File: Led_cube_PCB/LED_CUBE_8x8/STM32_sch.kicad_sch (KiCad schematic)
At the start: 23 parts, among them IC29 STM32C071C8T6, IC30 TPS562202DRLR, J2 20021121-00014T4LF, Y1 ABM11-48.000MHz-D7X-T

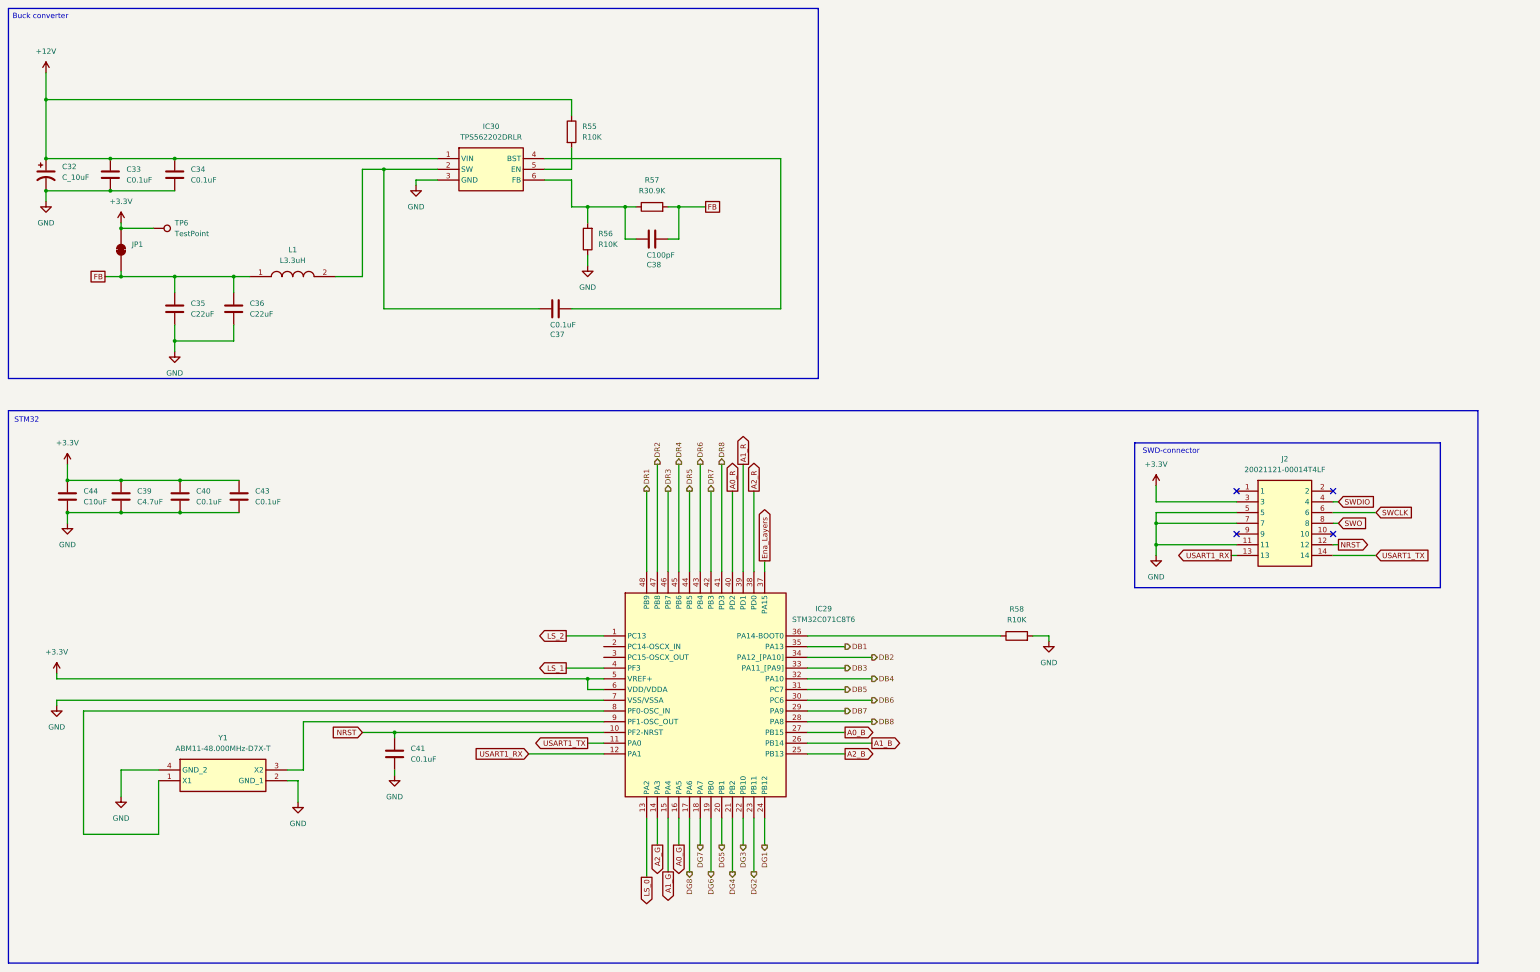
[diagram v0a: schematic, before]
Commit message: Finalized schematic changed power source and buck converter due to unavailability stock mouser. Also assigned all the footprints to all components and ran ERC.
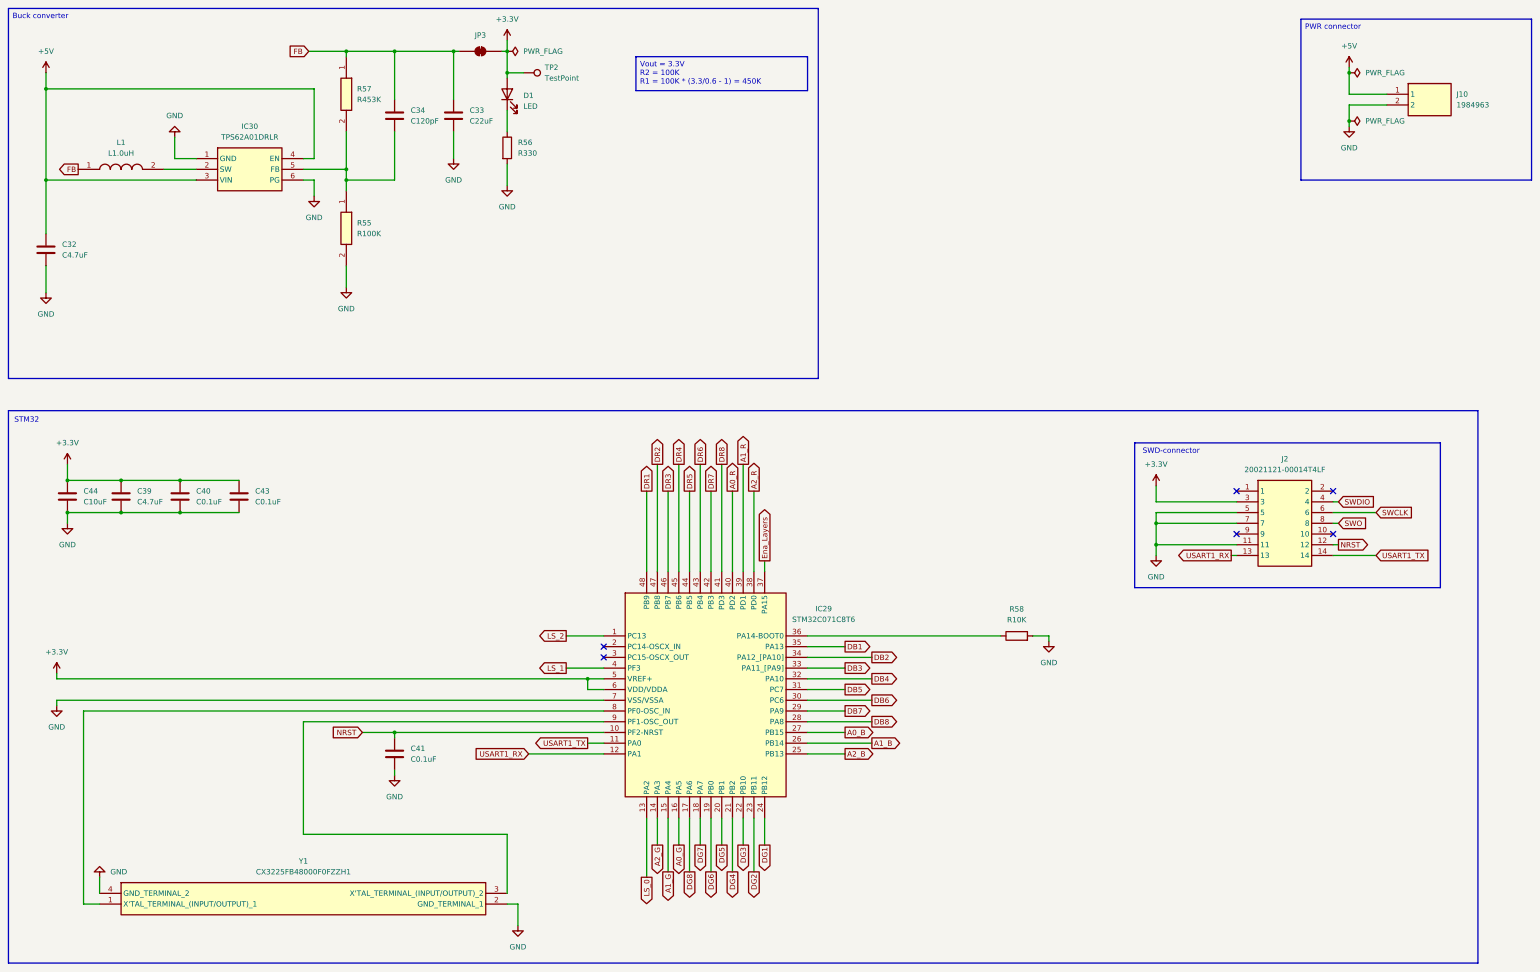
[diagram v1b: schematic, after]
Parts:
- removed C32: C_10uF, symbol Device:C_Polarized_US
- removed C35, C36: C22uF, symbol Device:C
- removed C37: C0.1uF, symbol Device:C
- removed C38: C100pF, symbol Device:C
- removed IC30: TPS562202DRLR, SOTFL50P160X60-6N, symbol SamacSys_Parts:TPS562202DRLR
- removed JP1: SolderJumper_2_Bridged, Jumper:SolderJumper-2_P1.3mm_Open_RoundedPad1.0x1.5mm, symbol Jumper:SolderJumper_2_Bridged
- removed L1: L3.3uH, BMRA000606303R3MA1, symbol SamacSys_Parts:BMRA000606303R3MA1
- removed R55: R10K, symbol Device:R
- removed R57: R30.9K, symbol Device:R
- removed TP6: TestPoint, TestPoint:TestPoint_Pad_D2.0mm, symbol Connector:TestPoint
- removed Y1: ABM11-48.000MHz-D7X-T, ABM11, symbol SamacSys_Parts:ABM11-48.000MHz-D7X-T
- added C32: C4.7uF, Capacitor_SMD:C_0805_2012Metric_Pad1.18x1.45mm_HandSolder, symbol Device:C
- added D1: LED, LED_SMD:LED_0805_2012Metric_Pad1.15x1.40mm_HandSolder, symbol Device:LED
- added IC30: TPS62A01DRLR, SamacSys_Parts:SOTFL50P160X60-6N, symbol SamacSys_Parts:TPS62A01DRLR
- added J10: 1984963, SamacSys_Parts:1984963, symbol SamacSys_Parts:1984963
- added JP3: SolderJumper_2_Bridged, Jumper:SolderJumper-2_P1.3mm_Open_RoundedPad1.0x1.5mm, symbol Jumper:SolderJumper_2_Bridged
- added L1: L1.0uH, SamacSys_Parts:DFE2HCAH1R0MJ0L, symbol SamacSys_Parts:DFE252012F-1R0M=P2
- added R55: R100K, Resistor_SMD:R_0805_2012Metric_Pad1.20x1.40mm_HandSolder, symbol SamacSys_Parts:RC0201FR-7D100KL
- added R57: R453K, Resistor_SMD:R_0805_2012Metric_Pad1.20x1.40mm_HandSolder, symbol SamacSys_Parts:RC0201FR-07453KL
- added TP2: TestPoint, TestPoint:TestPoint_Pad_D2.0mm, symbol Connector:TestPoint
- added Y1: CX3225FB48000F0FZZH1, SamacSys_Parts:CX3225FB48000F0FZZH1, symbol SamacSys_Parts:CX3225FB48000F0FZZH1
- C33: value C0.1uF -> C22uF; footprint (none) -> Capacitor_SMD:C_0805_2012Metric_Pad1.18x1.45mm_HandSolder
- C34: value C0.1uF -> C120pF; footprint (none) -> Capacitor_SMD:C_0805_2012Metric_Pad1.18x1.45mm_HandSolder
- C39, C40, C41, C43, C44: footprint (none) -> Capacitor_SMD:C_0805_2012Metric_Pad1.18x1.45mm_HandSolder
- IC29: footprint QFP50P900X900X160-48N -> SamacSys_Parts:QFP50P900X900X160-48N
- J2: footprint 2002112100014T4LF -> SamacSys_Parts:2002112100014T4LF
- R56: value R10K -> R330; footprint (none) -> Resistor_SMD:R_0805_2012Metric_Pad1.20x1.40mm_HandSolder
- R58: footprint (none) -> Resistor_SMD:R_0805_2012Metric_Pad1.20x1.40mm_HandSolder
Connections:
- net +12V is gone; now on net FB: C33.1, C34.1
- net +3.3V: now also D1.2 (A), JP3.1 (A), TP2.1
- net FB: now also JP3.2 (B), L1.1, R57.1
- net GND: now also R56.2, C32.2, IC30.1 (GND), IC30.6 (PG), J10.2, R55.2, Y1.2 (GND_TERMINAL_1), Y1.4 (GND_TERMINAL_2); no longer C34.2, R56.1
- net at IC29.8 (PF0-OSC_IN): now also Y1.1 (X'TAL_TERMINAL_(INPUT/OUTPUT)_1)
- net at IC29.9 (PF1-OSC_OUT): now also Y1.3 (X'TAL_TERMINAL_(INPUT/OUTPUT)_2)
- new net: C34.2, IC30.5 (FB), R55.1, R57.2
- new net: D1.1 (K), R56.1
- new net: IC30.2 (SW), L1.2
- new net +5V: C32.1, IC30.3 (VIN), IC30.4 (EN), J10.1
- no-connect marks 4 -> 6

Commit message: start of PCB layout
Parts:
- C32, C33, C34, C39, C40, C41, C43, C44: footprint Capacitor_SMD:C_0805_2012Metric_Pad1.18x1.45mm_HandSolder -> Capacitor_SMD:C_0603_1608Metric_Pad1.08x0.95mm_HandSolder
- R55: footprint Resistor_SMD:R_0805_2012Metric_Pad1.20x1.40mm_HandSolder -> Resistor_SMD:R_0603_1608Metric_Pad0.98x0.95mm_HandSolder; Manufacturer_Part_Number RC0201FR-7D100KL -> SR0603FR-07100KL; Mouser Part Number 603-RC0201FR-7D100KL -> 603-SR0603FR-07100KL; Mouser Price/Stock https://www.mouser.co.uk/ProductDetail/YAGEO/RC0201FR-7D100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 -> https://nl.mouser.com/en/ProductDetail/YAGEO/SR0603FR-07100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
- R56, R58: footprint Resistor_SMD:R_0805_2012Metric_Pad1.20x1.40mm_HandSolder -> Resistor_SMD:R_0603_1608Metric_Pad0.98x0.95mm_HandSolder
- R57: footprint Resistor_SMD:R_0805_2012Metric_Pad1.20x1.40mm_HandSolder -> Resistor_SMD:R_0603_1608Metric_Pad0.98x0.95mm_HandSolder; Manufacturer_Part_Number RC0201FR-07453KL -> AF0603FR-07453KL; Mouser Part Number 603-RC0201FR-07453KL -> 603-AF0603FR-07453KL; Mouser Price/Stock https://www.mouser.co.uk/ProductDetail/YAGEO/RC0201FR-07453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 -> https://nl.mouser.com/en/ProductDetail/YAGEO/AF0603FR-07453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
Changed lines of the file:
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@@
 			)
 		)
-		(property "Footprint" "Capacitor_SMD:C_0805_2012Metric_Pad1.18x1.45mm_HandSolder"
+		(property "Footprint" "Capacitor_SMD:C_0603_1608Metric_Pad1.08x0.95mm_HandSolder"
 			(at 56.8452 133.35 0)
 			(hide yes)
@@
 			)
 		)
-		(property "Footprint" "Resistor_SMD:R_0805_2012Metric_Pad1.20x1.40mm_HandSolder"
+		(property "Footprint" "Resistor_SMD:R_0603_1608Metric_Pad0.98x0.95mm_HandSolder"
 			(at -0.94 71.12 0)
 			(hide yes)
@@
 			)
 		)
-		(property "Datasheet" "http://www.yageo.com/documents/recent/PYu-RC0201_51_RoHS_L_8.pdf"
+		(property "Datasheet" ""
 			(at -100.94 71.12 0)
 			(hide yes)
@@
 			)
 		)
-		(property "Mouser Part Number" "603-RC0201FR-7D100KL"
+		(property "Mouser Part Number" "603-SR0603FR-07100KL"
 			(at -400.94 71.12 0)
 			(hide yes)
@@
 			)
 		)
-		(property "Mouser Price/Stock" "https://www.mouser.co.uk/ProductDetail/YAGEO/RC0201FR-7D100KL?qs=NgbZBzc1CyEJ6dcGr2%2F%252Bdg%3D%3D"
+		(property "Mouser Price/Stock" "https://nl.mouser.com/en/ProductDetail/YAGEO/SR0603FR-07100KL?qs=sGAEpiMZZMtG0KNrPCHnjRv1MJzRlXPZ3DN8ub9uSdtrODw9zR96PQ%3D%3D"
 			(at -500.94 71.12 0)
 			(hide yes)
@@
 			)
 		)
-		(property "Manufacturer_Part_Number" "RC0201FR-7D100KL"
+		(property "Manufacturer_Part_Number" "SR0603FR-07100KL"
 			(at -700.94 71.12 0)
 			(hide yes)
@@
 			)
 		)
-		(property "Footprint" "Capacitor_SMD:C_0805_2012Metric_Pad1.18x1.45mm_HandSolder"
+		(property "Footprint" "Capacitor_SMD:C_0603_1608Metric_Pad1.08x0.95mm_HandSolder"
 			(at 107.6452 194.31 0)
 			(hide yes)
@@
 			)
 		)
-		(property "Footprint" "Capacitor_SMD:C_0805_2012Metric_Pad1.18x1.45mm_HandSolder"
+		(property "Footprint" "Capacitor_SMD:C_0603_1608Metric_Pad1.08x0.95mm_HandSolder"
 			(at 42.8752 133.35 0)
 			(hide yes)
@@
 			)
 		)
-		(property "Footprint" "Resistor_SMD:R_0805_2012Metric_Pad1.20x1.40mm_HandSolder"
+		(property "Footprint" "Resistor_SMD:R_0603_1608Metric_Pad0.98x0.95mm_HandSolder"
 			(at 254 164.338 90)
 			(hide yes)
@@
 			)
 		)
-		(property "Footprint" "Capacitor_SMD:C_0805_2012Metric_Pad1.18x1.45mm_HandSolder"
+		(property "Footprint" "Capacitor_SMD:C_0603_1608Metric_Pad1.08x0.95mm_HandSolder"
 			(at 70.8152 133.35 0)
 			(hide yes)
@@
 			)
 		)
-		(property "Footprint" "Capacitor_SMD:C_0805_2012Metric_Pad1.18x1.45mm_HandSolder"
+		(property "Footprint" "Capacitor_SMD:C_0603_1608Metric_Pad1.08x0.95mm_HandSolder"
 			(at 25.0952 74.93 0)
 			(hide yes)
@@
 			)
 		)
-		(property "Footprint" "Capacitor_SMD:C_0805_2012Metric_Pad1.18x1.45mm_HandSolder"
+		(property "Footprint" "Capacitor_SMD:C_0603_1608Metric_Pad1.08x0.95mm_HandSolder"
 			(at 107.6452 43.18 0)
 			(hide yes)
@@
 			)
 		)
-		(property "Footprint" "Capacitor_SMD:C_0805_2012Metric_Pad1.18x1.45mm_HandSolder"
+		(property "Footprint" "Capacitor_SMD:C_0603_1608Metric_Pad1.08x0.95mm_HandSolder"
 			(at 121.6152 43.18 0)
 			(hide yes)
@@
 			)
 		)
-		(property "Footprint" "Capacitor_SMD:C_0805_2012Metric_Pad1.18x1.45mm_HandSolder"
+		(property "Footprint" "Capacitor_SMD:C_0603_1608Metric_Pad1.08x0.95mm_HandSolder"
 			(at 30.1752 133.35 0)
 			(hide yes)
@@
 			)
 		)
-		(property "Footprint" "Resistor_SMD:R_0805_2012Metric_Pad1.20x1.40mm_HandSolder"
+		(property "Footprint" "Resistor_SMD:R_0603_1608Metric_Pad0.98x0.95mm_HandSolder"
 			(at 131.572 46.99 90)
 			(hide yes)
@@
 			)
 		)
-		(property "Footprint" "Resistor_SMD:R_0805_2012Metric_Pad1.20x1.40mm_HandSolder"
+		(property "Footprint" "Resistor_SMD:R_0603_1608Metric_Pad0.98x0.95mm_HandSolder"
 			(at -0.94 39.37 0)
 			(hide yes)
@@
 			)
 		)
-		(property "Datasheet" "https://www.yageo.com/upload/media/product/products/datasheet/rchip/PYu-RC_Group_51_RoHS_L_12.pdf"
+		(property "Datasheet" "chrome-extension://efaidnbmnnnibpcajpcglclefindmkaj/https://nl.mouser.com/datasheet/3/508/1/PYu-AF_51_RoHS_L_9.pdf"
 			(at -100.94 39.37 0)
 			(hide yes)
@@
 			)
 		)
-		(property "Mouser Part Number" "603-RC0201FR-07453KL"
+		(property "Mouser Part Number" "603-AF0603FR-07453KL"
 			(at -400.94 39.37 0)
 			(hide yes)
@@
 			)
 		)
-		(property "Mouser Price/Stock" "https://www.mouser.co.uk/ProductDetail/YAGEO/RC0201FR-07453KL?qs=1s%252BlIcjv25sZ2i87AF%252BnmQ%3D%3D"
+		(property "Mouser Price/Stock" "https://nl.mouser.com/en/ProductDetail/YAGEO/AF0603FR-07453KL?qs=sGAEpiMZZMtlubZbdhIBIK%252BAKCop5cydMz3xptmMHDE%3D"
 			(at -500.94 39.37 0)
 			(hide yes)
@@
 			)
 		)
-		(property "Manufacturer_Part_Number" "RC0201FR-07453KL"
+		(property "Manufacturer_Part_Number" "AF0603FR-07453KL"
 			(at -700.94 39.37 0)
 			(hide yes)

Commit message: Top layer placement done revised the SWD connector and started routing.
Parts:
- removed C44: C10uF, Capacitor_SMD:C_0603_1608Metric_Pad1.08x0.95mm_HandSolder, symbol Device:C
- removed J2: 20021121-00014T4LF, SamacSys_Parts:2002112100014T4LF, symbol SamacSys_Parts:20021121-00014T4LF
- removed R58: R10K, Resistor_SMD:R_0603_1608Metric_Pad0.98x0.95mm_HandSolder, symbol Device:R
- added J1: FTSH-107-01-L-DV-K-A, FTSH-107-XX-YYY-DV-K-A, symbol SamacSys_Parts:FTSH-107-01-L-DV-K-A
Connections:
- net +3.3V: now also J1.3
- net DB1: now also IC29.2 (PC14-OSCX_IN); no longer IC29.35 (PA13)
- net GND: now also J1.11, J1.5, J1.7
- net NRST: now also J1.12
- net SWCLK: now also IC29.36 (PA14-BOOT0), J1.6
- net SWDIO: now also IC29.35 (PA13), J1.4
- net USART1_RX: now also IC29.11 (PA0), J1.13; no longer IC29.12 (PA1)
- net USART1_TX: now also IC29.12 (PA1), J1.14; no longer IC29.11 (PA0)
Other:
- moved on the sheet: C39, C40, C41
